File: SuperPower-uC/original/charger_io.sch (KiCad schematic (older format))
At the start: 24 parts, among them J8 Barrel_Jack_Switch, J9 DNP/Screw_Terminal_01x02, Q8 DMP3028LSD, U3 USB-C, U9 IP4220CZ6

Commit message: Re-Annotate project
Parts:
- renumbered D4 to D1, D5 to D2, H3 to H2, H2 to H3, J8 to J2, J9 to J3, LED2 to LED1, Q8 to Q2, R38 to R10, R39 to R11, R33 to R4, R34 to R5, R35 to R6, R36 to R7, R4 to R8, R37 to R9, TP19 to TP4, TP20 to TP5, TP21 to TP6, TP22 to TP7, U3 to U2, U9 to U3

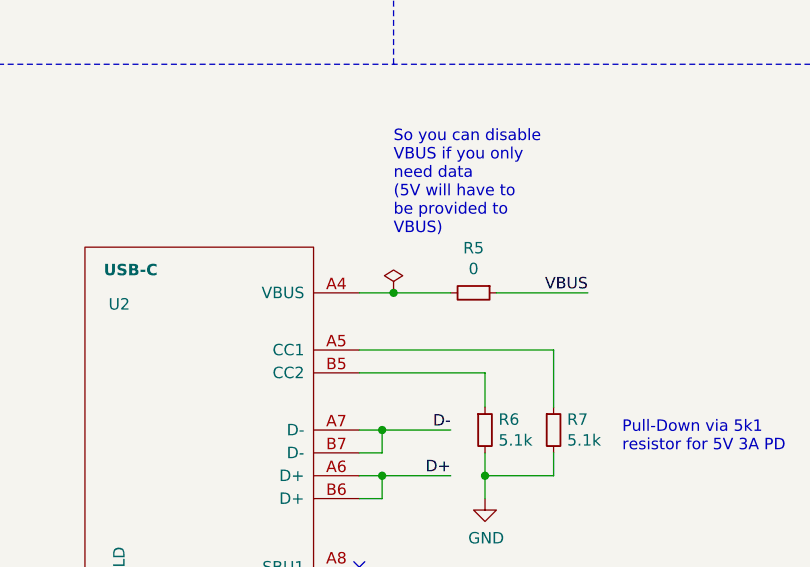
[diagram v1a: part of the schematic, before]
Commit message: Fix more ERC issues
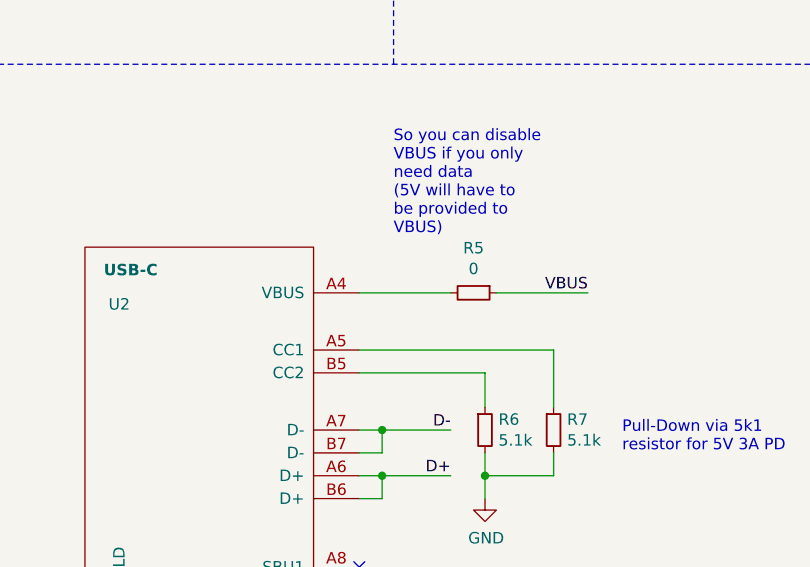
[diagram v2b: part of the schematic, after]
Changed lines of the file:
@@
 Wire Wire Line
 	4100 5050 3700 5050
-Wire Wire Line
-	3500 5050 3250 5050
 $Comp
 L Device:R_Small R5
@@
 Wire Notes Line
 	550  2000 550  550
-$Comp
-L power:PWR_FLAG #FLG04
-U 1 1 5FDD7D70
-P 3250 5050
-F 0 "#FLG04" H 3250 5125 50  0001 C CNN
-F 1 "PWR_FLAG" H 3250 5223 50  0001 C CNN
-F 2 "" H 3250 5050 50  0001 C CNN
-F 3 "~" H 3250 5050 50  0001 C CNN
-	1    3250 5050
-	1    0    0    -1
-$EndComp
-Connection ~ 3250 5050
-Wire Wire Line
-	3250 5050 3100 5050
 $Comp
 L usb-c:USB-C U2
@@
 Wire Wire Line
 	2250 3500 2250 3400
+Wire Wire Line
+	3100 5050 3500 5050
 $EndSCHEMATC

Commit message: Add 3D file to every component
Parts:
- J2: footprint Connector_BarrelJack:BarrelJack_Horizontal -> Connector_BarrelJack:BarrelJack_CUI_PJ-102AH_Horizontal
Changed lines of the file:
@@
 F 0 "J2" H 4257 3317 50  0000 C CNN
 F 1 "Barrel_Jack_Switch" H 4257 3226 50  0000 C CNN
-F 2 "Connector_BarrelJack:BarrelJack_Horizontal" H 4250 2960 50  0001 C CNN
+F 2 "Connector_BarrelJack:BarrelJack_CUI_PJ-102AH_Horizontal" H 4250 2960 50  0001 C CNN
 F 3 "~" H 4250 2960 50  0001 C CNN
 	1    4200 3000

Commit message: Remove R40 + Update Terminal Block Footprint
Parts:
- J3: footprint Connector_PinSocket_2.54mm:PinSocket_1x02_P2.54mm_Vertical -> TerminalBlock_Phoenix:TerminalBlock_Phoenix_MKDS-1,5-2_1x02_P5.00mm_Horizontal
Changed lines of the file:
@@
 F 0 "J3" H 6718 2825 50  0000 C CNN
 F 1 "DNP/Screw_Terminal_01x02" H 6718 2916 50  0000 C CNN
-F 2 "Connector_PinSocket_2.54mm:PinSocket_1x02_P2.54mm_Vertical" H 6800 3150 50  0001 C CNN
+F 2 "TerminalBlock_Phoenix:TerminalBlock_Phoenix_MKDS-1,5-2_1x02_P5.00mm_Horizontal" H 6800 3150 50  0001 C CNN
 F 3 "~" H 6800 3150 50  0001 C CNN
 	1    6800 3150

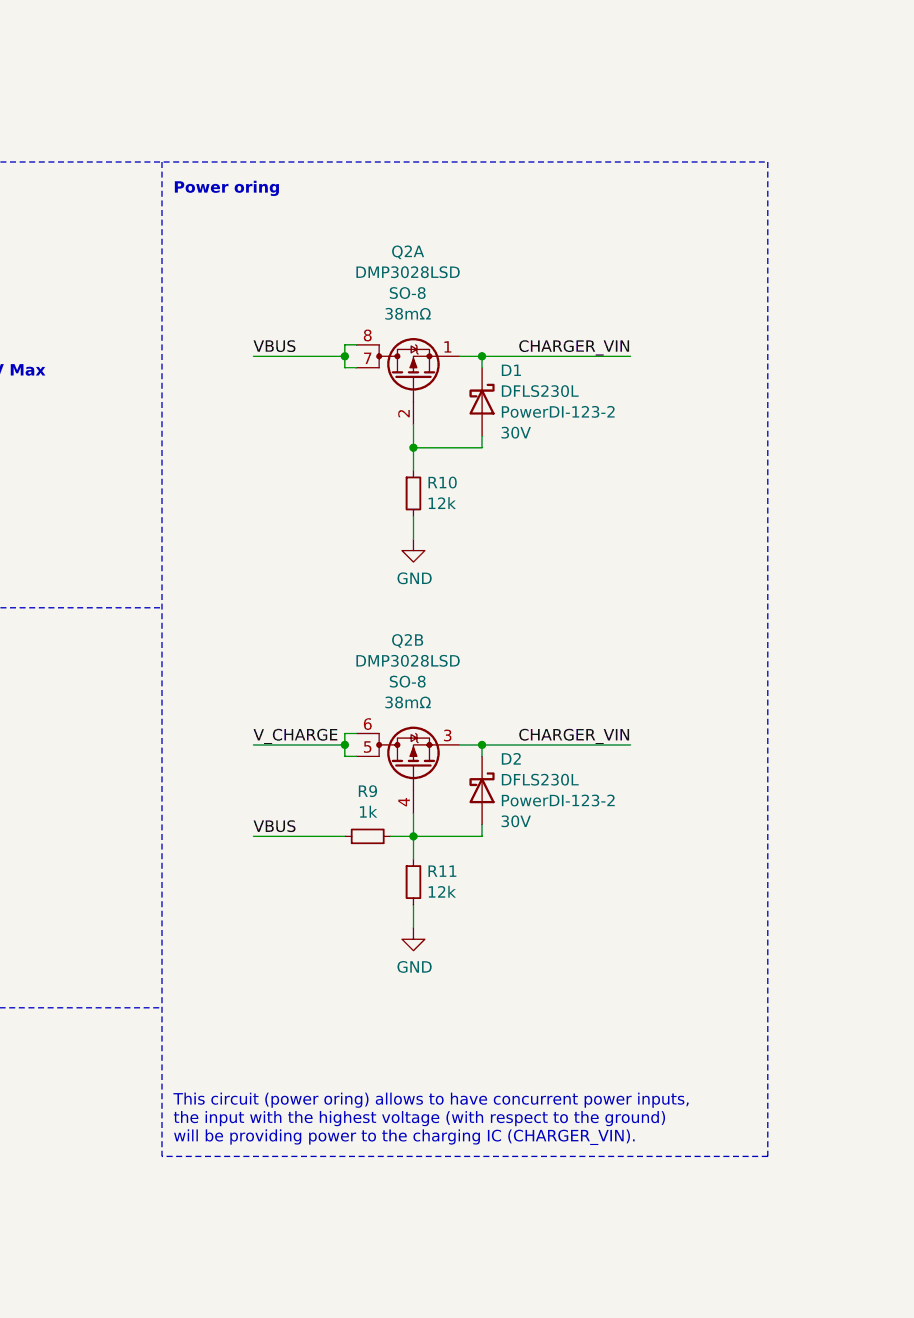
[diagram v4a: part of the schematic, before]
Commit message: Change ORing topology
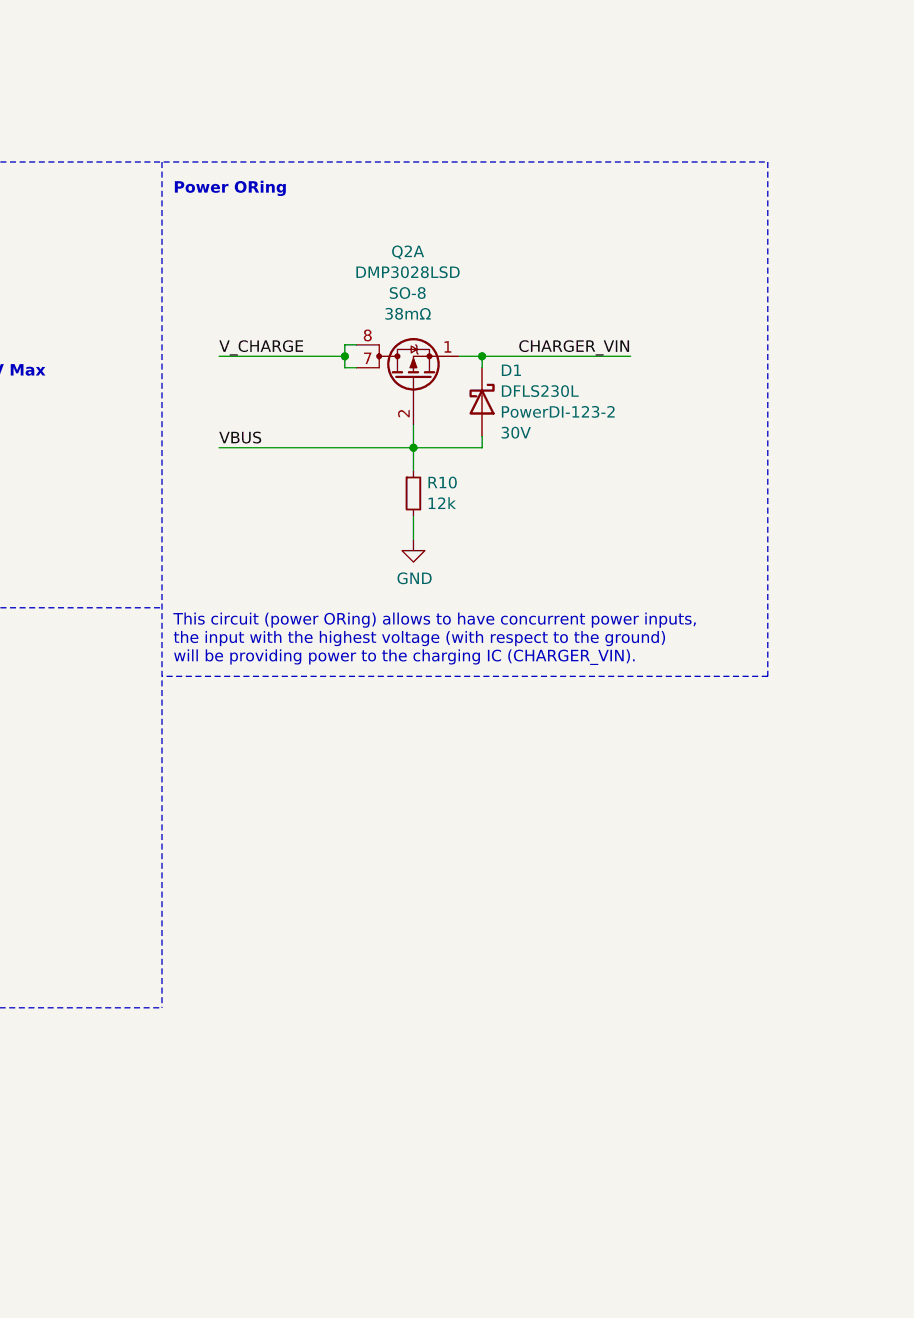
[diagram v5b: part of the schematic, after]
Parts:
- removed D2: DFLS230L, Diode_SMD:D_PowerDI-123, symbol dfls230l:DFLS230L
- removed unit 2 of Q2
- removed R11: 12k, Resistor_SMD:R_0603_1608Metric, symbol Device:R_Small
- removed R9: 1k, Resistor_SMD:R_0603_1608Metric, symbol Device:R_Small
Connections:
- net VBUS: now also D1.2 (A), Q2.2 (G), R10.1; no longer Q2.7 (D), Q2.8 (D)
- net V_CHARGE: now also Q2.7 (D), Q2.8 (D)
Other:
- note added: "Power ORing"
- note added: "This circuit (power ORing) allows to have concurrent power inputs,\nthe input with the highest voltage (with respect to the ground)\nwill be providing power to the charging IC (CHARGER_VIN)."
- note removed: "Power oring"
- note removed: "This circuit (power oring) allows to have concurrent power inputs,\nthe input with the highest voltage (with respect to the ground)\nwill be providing power to the charging IC (CHARGER_VIN)."

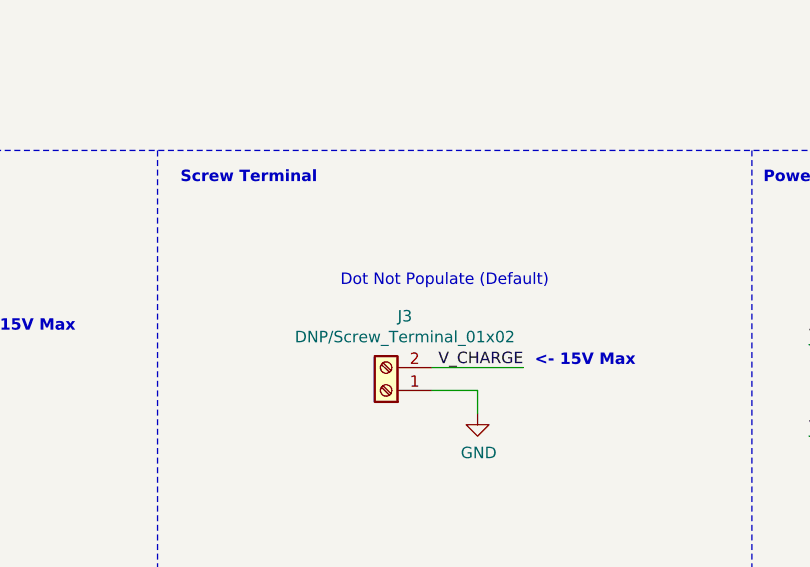
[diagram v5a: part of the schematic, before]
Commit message: Add new footprint for external input pads instead of screw terminal
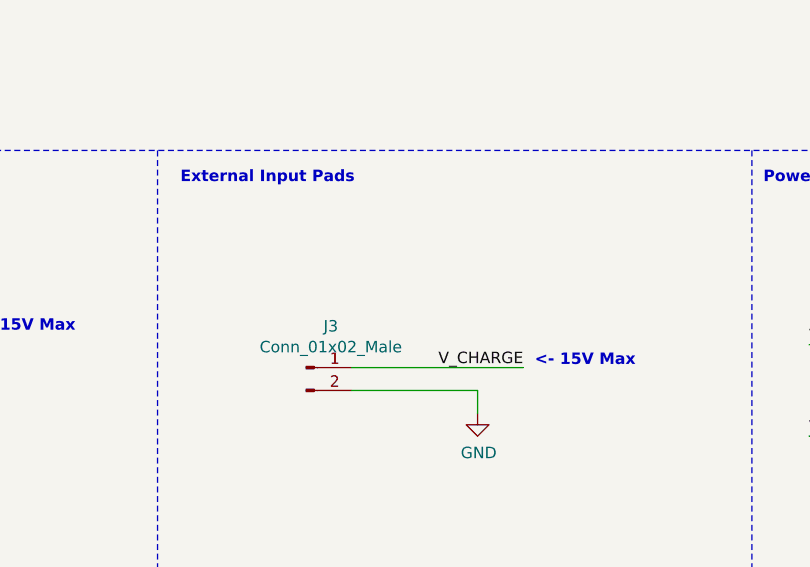
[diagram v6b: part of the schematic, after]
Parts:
- removed J3: DNP/Screw_Terminal_01x02, TerminalBlock_Phoenix:TerminalBlock_Phoenix_MKDS-1,5-2_1x02_P5.00mm_Horizontal, symbol Connector:Screw_Terminal_01x02
- added J3: Conn_01x02_Male, ext_input:ext_input_pads, symbol Connector:Conn_01x02_Male
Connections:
- net GND: now also J3.2 (Pin_2)
- net V_CHARGE: now also J3.1 (Pin_1)
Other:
- note added: "External Input Pads"
- note removed: "Dot Not Populate (Default)"
- note removed: "Screw Terminal"
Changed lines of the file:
@@
 Text Label 4950 2900 2    50   ~ 0
 V_CHARGE
-$Comp
-L Connector:Screw_Terminal_01x02 J3
-U 1 1 5F74DB0F
-P 6800 3150
-F 0 "J3" H 6718 2825 50  0000 C CNN
-F 1 "DNP/Screw_Terminal_01x02" H 6718 2916 50  0000 C CNN
-F 2 "TerminalBlock_Phoenix:TerminalBlock_Phoenix_MKDS-1,5-2_1x02_P5.00mm_Horizontal" H 6800 3150 50  0001 C CNN
-F 3 "~" H 6800 3150 50  0001 C CNN
-	1    6800 3150
-	-1   0    0    1
-$EndComp
 Text Label 7400 3050 2    50   ~ 0
 V_CHARGE
@@
 Wire Wire Line
 	7200 3250 7200 3150
-Wire Wire Line
-	7200 3150 7000 3150
-Wire Wire Line
-	7000 3050 7400 3050
 Text Notes 3350 2250 0    50   ~ 10
 Barrel Jack\n
 Text Notes 5900 2250 0    50   ~ 10
-Screw Terminal
+External Input Pads
 Wire Notes Line
 	5800 7450 1100 7450
@@
 Text Notes 7450 3050 0    50   ~ 10
 <- 15V Max
-Text Notes 6600 2700 0    50   ~ 0
-Dot Not Populate (Default)
 $Comp
 L Mechanical:MountingHole_Pad H1
@@
 Wire Notes Line
 	11050 4350 8400 4350
+$Comp
+L Connector:Conn_01x02_Male J3
+U 1 1 5FF39CF2
+P 6450 3050
+F 0 "J3" H 6558 3231 50  0000 C CNN
+F 1 "Conn_01x02_Male" H 6558 3140 50  0000 C CNN
+F 2 "ext_input:ext_input_pads" H 6450 3050 50  0001 C CNN
+F 3 "~" H 6450 3050 50  0001 C CNN
+	1    6450 3050
+	1    0    0    -1
+$EndComp
+Wire Wire Line
+	6650 3050 7400 3050
+Wire Wire Line
+	6650 3150 7200 3150
 $EndSCHEMATC

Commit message: Rename some MOSFETs symbol fields
+ Update libraries
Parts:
- Q2: IDmax 4.7A -> (none); RDSon 38mΩ -> (none); Release_date 2020-12-13 -> 2020-12-21; Release_version 1.02 -> 1.03; Type P + P -> (none); VDSS 30V -> (none); VGSS 20V -> (none); VGSth 1-3V -> (none); mos_IDmax (none) -> 4.7A; mos_RDSon (none) -> 38mΩ; mos_Type (none) -> P + P; mos_VDSS (none) -> 30V; mos_VGSS (none) -> 20V; mos_VGSth (none) -> 1-3V
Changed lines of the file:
@@
 F 5 "DMP3028LSD-13" H 9500 3050 50  0001 C CNN "Mfr_no"
 F 6 "SO-8" V 9875 3075 50  0000 C CNN "Package"
-F 7 "P + P" H 9500 3050 50  0001 C CNN "Type"
-F 8 "30V" H 9500 3050 50  0001 C CNN "VDSS"
-F 9 "38mΩ" V 9784 3075 50  0000 C CNN "RDSon"
-F 10 "4.7A" H 9500 3050 50  0001 C CNN "IDmax"
-F 11 "1-3V" H 9500 3050 50  0001 C CNN "VGSth"
-F 12 "20V" H 9500 3050 50  0001 C CNN "VGSS"
+F 7 "P + P" H 9500 3050 50  0001 C CNN "mos_Type"
+F 8 "30V" H 9500 3050 50  0001 C CNN "mos_VDSS"
+F 9 "38mΩ" V 9784 3075 50  0000 C CNN "mos_RDSon"
+F 10 "4.7A" H 9500 3050 50  0001 C CNN "mos_IDmax"
+F 11 "1-3V" H 9500 3050 50  0001 C CNN "mos_VGSth"
+F 12 "20V" H 9500 3050 50  0001 C CNN "mos_VGSS"
 F 13 "https://octopart.com/dmp3028lsd-13-diodes+inc.-67250487?r=sp" H 9500 3050 50  0001 C CNN "Octopart_link"
 F 14 "-" H 9500 3050 50  0001 C CNN "Farnell_link"
@@
 F 45 "-" H 9500 3050 50  0001 C CNN "RS_stock"
 F 46 "TO_CHECK" H 9500 3050 50  0001 C CNN "Status"
-F 47 "1.02" H 9500 3050 50  0001 C CNN "Release_version"
-F 48 "2020-12-13" H 9500 3050 50  0001 C CNN "Release_date"
+F 47 "1.03" H 9500 3050 50  0001 C CNN "Release_version"
+F 48 "2020-12-21" H 9500 3050 50  0001 C CNN "Release_date"
 F 49 "ManWithNoName" H 9500 3050 50  0001 C CNN "Designer"
 	1    9500 3050

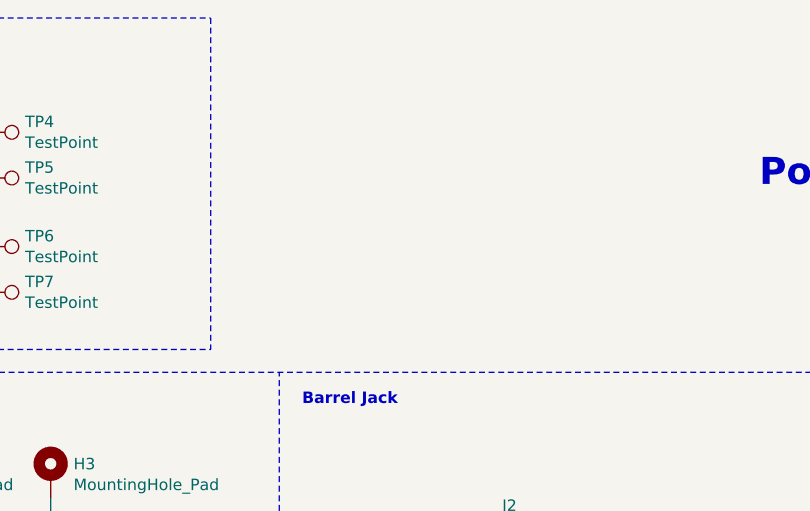
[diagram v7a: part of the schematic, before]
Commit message: Solve the 2 ERC issues
Update the common pin type of the 3 ways solder jumper (replace "input" by "passive") + Add a Power Flag to GND on "Power IO" sheet
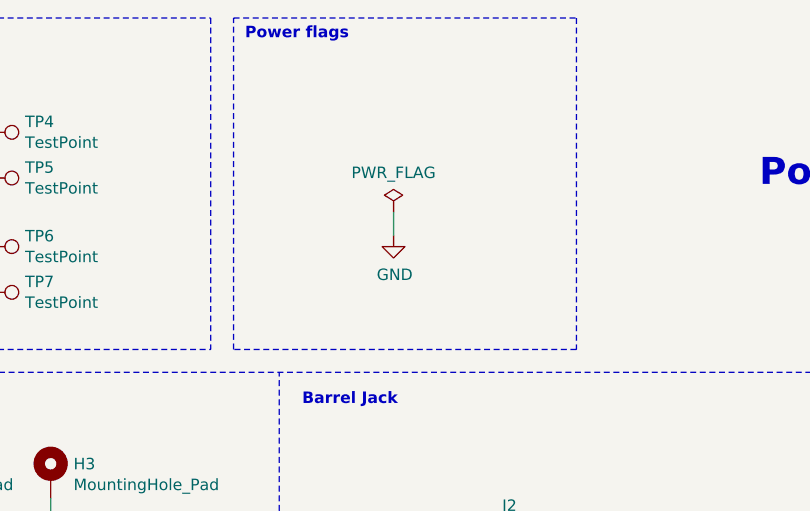
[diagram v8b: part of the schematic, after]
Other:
- note added: "Power flags"
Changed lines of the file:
@@
 	1    0    0    -1
 $EndComp
-$Comp
-L power:GND #PWR014
-U 1 1 5FDED30D
-P 2250 3500
-F 0 "#PWR014" H 2250 3250 50  0001 C CNN
-F 1 "GND" H 2255 3327 50  0000 C CNN
-F 2 "" H 2250 3500 50  0001 C CNN
-F 3 "" H 2250 3500 50  0001 C CNN
-	1    2250 3500
-	1    0    0    -1
-$EndComp
-Wire Wire Line
-	2250 3500 2250 3400
 Wire Wire Line
 	3100 5050 3500 5050
@@
 Wire Wire Line
 	6650 3150 7200 3150
+$Comp
+L power:GND #PWR0105
+U 1 1 5FE15B7B
+P 2250 3500
+F 0 "#PWR0105" H 2250 3250 50  0001 C CNN
+F 1 "GND" H 2255 3327 50  0000 C CNN
+F 2 "" H 2250 3500 50  0001 C CNN
+F 3 "" H 2250 3500 50  0001 C CNN
+	1    2250 3500
+	1    0    0    -1
+$EndComp
+Wire Wire Line
+	2250 3500 2250 3400
+$Comp
+L power:GND #PWR0106
+U 1 1 5FE186B3
+P 3750 1500
+F 0 "#PWR0106" H 3750 1250 50  0001 C CNN
+F 1 "GND" H 3755 1327 50  0000 C CNN
+F 2 "" H 3750 1500 50  0001 C CNN
+F 3 "" H 3750 1500 50  0001 C CNN
+	1    3750 1500
+	1    0    0    -1
+$EndComp
+$Comp
+L power:PWR_FLAG #FLG0101
+U 1 1 5FE193A0
+P 3750 1400
+F 0 "#FLG0101" H 3750 1475 50  0001 C CNN
+F 1 "PWR_FLAG" H 3750 1573 50  0000 C CNN
+F 2 "" H 3750 1400 50  0001 C CNN
+F 3 "~" H 3750 1400 50  0001 C CNN
+	1    3750 1400
+	1    0    0    -1
+$EndComp
+Wire Wire Line
+	3750 1400 3750 1500
+Wire Notes Line
+	3050 550  4550 550
+Wire Notes Line
+	4550 550  4550 2000
+Wire Notes Line
+	4550 2000 3050 2000
+Wire Notes Line
+	3050 2000 3050 550
+Text Notes 3100 650  0    50   ~ 10
+Power flags
 $EndSCHEMATC
